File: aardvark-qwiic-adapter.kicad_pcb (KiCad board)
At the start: 2 copper layers, 22.9 x 20.3 mm, 7 parts, among them J1 Conn_02x05_Odd_Even, J2 Conn_01x04, J3 Conn_01x04, J4 Conn_01x02, U1 AP7361C-33E

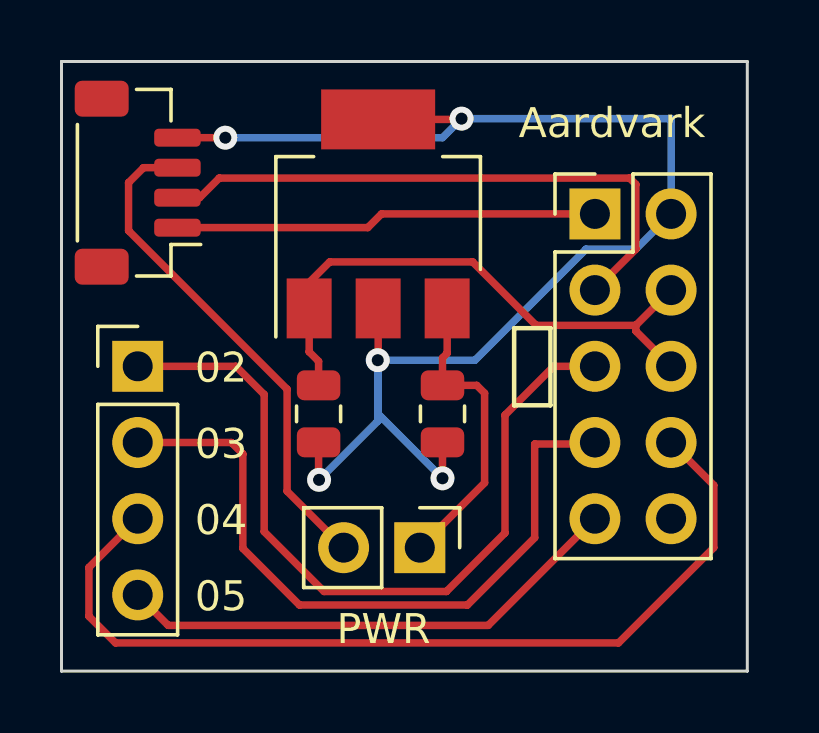
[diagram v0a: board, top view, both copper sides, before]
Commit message: PCB layout tweaks and silkscreen
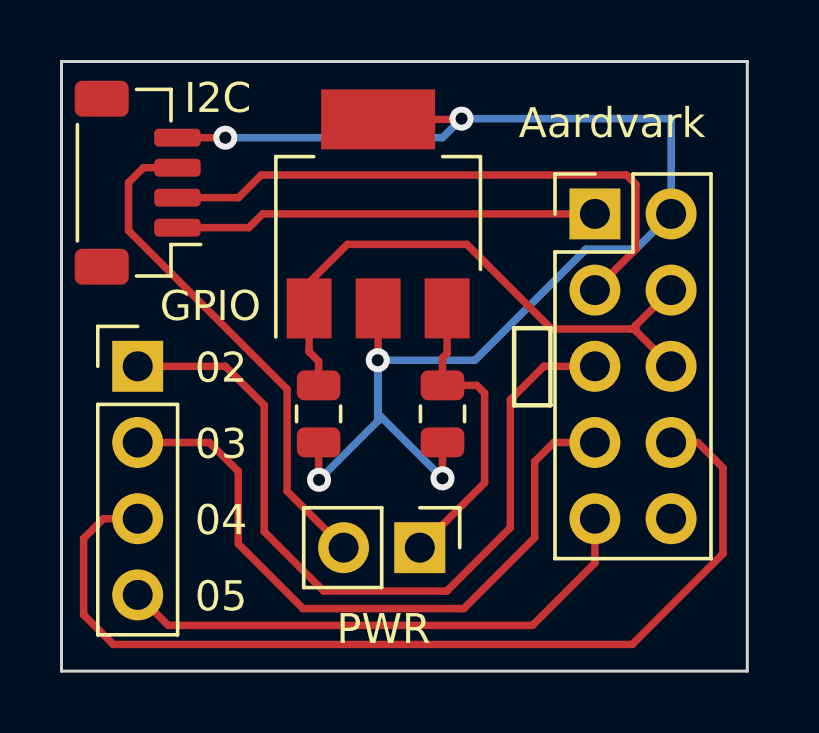
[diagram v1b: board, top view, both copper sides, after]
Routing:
- net /GPIO04: track 30.5 -> 32.5 mm
- net /GPIO05: track 17.1 -> 18.0 mm
- net /GPIO03: track 23.4 -> 22.7 mm
- net +5V: track 19.1 -> 19.7 mm
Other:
- board text added: "GPIO"
- board text added: "I2C"

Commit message: Clean up ground plance
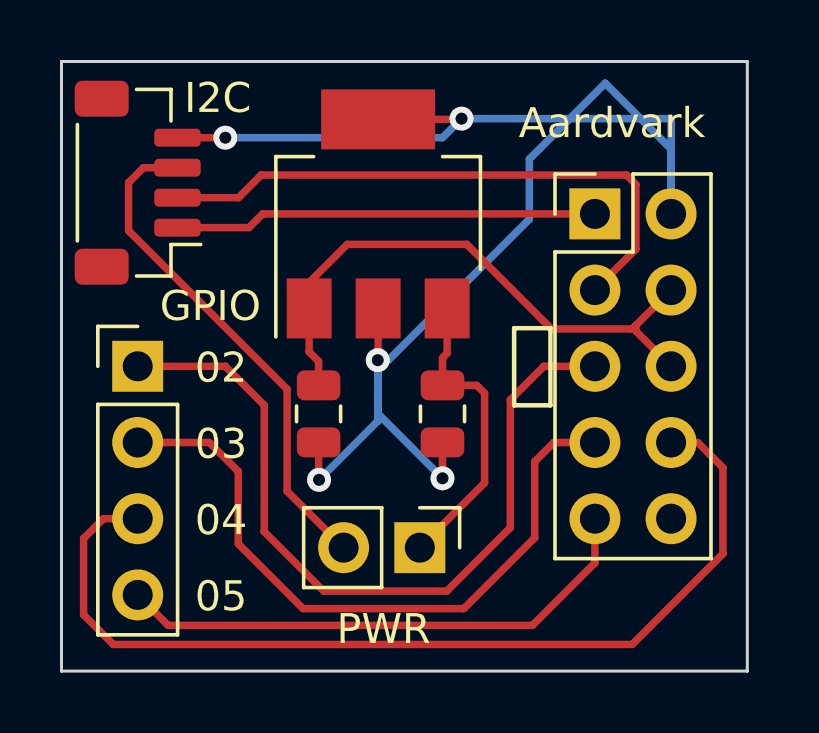
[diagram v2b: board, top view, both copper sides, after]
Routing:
- net GND: track 48.3 -> 54.3 mm
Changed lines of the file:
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@@
   (via (at 119.761 78.74) (size 0.8) (drill 0.4) (layers "F.Cu" "B.Cu") (net 3))
   (via (at 124.841 86.1568) (size 0.8) (drill 0.4) (layers "F.Cu" "B.Cu") (net 3))
+  (segment (start 129.8956 81.4578) (end 129.8956 79.4512) (width 0.25) (layer "B.Cu") (net 3))
   (segment (start 122.8852 90.1446) (end 124.841 88.1888) (width 0.25) (layer "B.Cu") (net 3))
   (segment (start 134.62 78.105) (end 134.62 81.28) (width 0.25) (layer "B.Cu") (net 3))
-  (segment (start 133.445 82.455) (end 134.62 81.28) (width 0.25) (layer "B.Cu") (net 3))
+  (segment (start 129.8956 79.4512) (end 132.4229 76.9239) (width 0.25) (layer "B.Cu") (net 3))
+  (segment (start 134.62 79.121) (end 134.62 81.28) (width 0.25) (layer "B.Cu") (net 3))
   (segment (start 124.841 88.1888) (end 124.841 86.1568) (width 0.25) (layer "B.Cu") (net 3))
+  (segment (start 125.1966 86.1568) (end 129.8956 81.4578) (width 0.25) (layer "B.Cu") (net 3))
+  (segment (start 124.841 86.1568) (end 125.1966 86.1568) (width 0.25) (layer "B.Cu") (net 3))
   (segment (start 127 78.74) (end 127.635 78.105) (width 0.25) (layer "B.Cu") (net 3))
   (segment (start 124.841 87.9348) (end 124.841 86.1568) (width 0.25) (layer "B.Cu") (net 3))
-  (segment (start 124.841 86.1568) (end 128.081499 86.1568) (width 0.25) (layer "B.Cu") (net 3))
   (segment (start 119.761 78.74) (end 127 78.74) (width 0.25) (layer "B.Cu") (net 3))
-  (segment (start 128.081499 86.1568) (end 131.783299 82.455) (width 0.25) (layer "B.Cu") (net 3))
+  (segment (start 132.4229 76.9239) (end 134.62 79.121) (width 0.25) (layer "B.Cu") (net 3))
   (segment (start 127.635 78.105) (end 134.62 78.105) (width 0.25) (layer "B.Cu") (net 3))
   (segment (start 127 90.0938) (end 124.841 87.9348) (width 0.25) (layer "B.Cu") (net 3))
-  (segment (start 131.783299 82.455) (end 133.445 82.455) (width 0.25) (layer "B.Cu") (net 3))
   (segment (start 126.243 92.4052) (end 128.4042 90.244) (width 0.25) (layer "F.Cu") (net 4))
   (segment (start 127.155 85.9256) (end 127.155 84.43) (width 0.25) (layer "F.Cu") (net 4))

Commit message: Tweak layout
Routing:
- net +3.3V: track 10.2 -> 10.9 mm
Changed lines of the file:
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@@
   (segment (start 121.0056 81.28) (end 120.5484 81.7372) (width 0.25) (layer "F.Cu") (net 1))
   (segment (start 120.5484 81.7372) (end 118.1678 81.7372) (width 0.25) (layer "F.Cu") (net 1))
-  (segment (start 132.08 83.82) (end 133.445 82.455) (width 0.25) (layer "F.Cu") (net 2))
+  (segment (start 133.1346 79.9846) (end 120.9548 79.9846) (width 0.25) (layer "F.Cu") (net 2))
+  (segment (start 132.08 83.82) (end 133.35 82.55) (width 0.25) (layer "F.Cu") (net 2))
+  (segment (start 133.35 80.2) (end 133.1346 79.9846) (width 0.25) (layer "F.Cu") (net 2))
+  (segment (start 133.35 82.55) (end 133.35 80.2) (width 0.25) (layer "F.Cu") (net 2))
+  (segment (start 120.9548 79.9846) (end 120.1994 80.74) (width 0.25) (layer "F.Cu") (net 2))
   (segment (start 120.1994 80.74) (end 118.165 80.74) (width 0.25) (layer "F.Cu") (net 2))
-  (segment (start 133.445 82.455) (end 133.445 80.295) (width 0.25) (layer "F.Cu") (net 2))
-  (segment (start 133.1346 79.9846) (end 120.9548 79.9846) (width 0.25) (layer "F.Cu") (net 2))
-  (segment (start 120.9548 79.9846) (end 120.1994 80.74) (width 0.25) (layer "F.Cu") (net 2))
-  (segment (start 133.445 80.295) (end 133.1346 79.9846) (width 0.25) (layer "F.Cu") (net 2))
   (segment (start 118.165 78.74) (end 119.761 78.74) (width 0.25) (layer "F.Cu") (net 3))
   (segment (start 122.87 88.895) (end 122.87 90.1294) (width 0.25) (layer "F.Cu") (net 3))
@@
   (segment (start 127.635 78.105) (end 134.62 78.105) (width 0.25) (layer "B.Cu") (net 3))
   (segment (start 127 90.0938) (end 124.841 87.9348) (width 0.25) (layer "B.Cu") (net 3))
-  (segment (start 126.243 92.4052) (end 128.4042 90.244) (width 0.25) (layer "F.Cu") (net 4))
   (segment (start 127.155 85.9256) (end 127.155 84.43) (width 0.25) (layer "F.Cu") (net 4))
-  (segment (start 128.4042 90.244) (end 128.4042 87.2562) (width 0.25) (layer "F.Cu") (net 4))
-  (segment (start 128.143 86.995) (end 127 86.995) (width 0.25) (layer "F.Cu") (net 4))
+  (segment (start 126.243 92.4052) (end 127.4826 92.4052) (width 0.25) (layer "F.Cu") (net 4))
+  (segment (start 128.4042 91.4836) (end 128.4042 87.2562) (width 0.25) (layer "F.Cu") (net 4))
   (segment (start 127 86.0806) (end 127.155 85.9256) (width 0.25) (layer "F.Cu") (net 4))
   (segment (start 128.4042 87.2562) (end 128.143 86.995) (width 0.25) (layer "F.Cu") (net 4))
+  (segment (start 128.143 86.995) (end 127 86.995) (width 0.25) (layer "F.Cu") (net 4))
+  (segment (start 127.4826 92.4052) (end 128.4042 91.4836) (width 0.25) (layer "F.Cu") (net 4))
   (segment (start 127 86.995) (end 127 86.0806) (width 0.25) (layer "F.Cu") (net 4))
-  (segment (start 121.0564 91.8718) (end 121.0564 87.6554) (width 0.25) (layer "F.Cu") (net 5))
   (segment (start 132.08 86.36) (end 130.3782 86.36) (width 0.25) (layer "F.Cu") (net 5))
+  (segment (start 130.3782 86.36) (end 129.2606 87.4776) (width 0.25) (layer "F.Cu") (net 5))
+  (segment (start 129.2606 87.4776) (end 129.2606 91.7376) (width 0.25) (layer "F.Cu") (net 5))
+  (segment (start 119.761 86.36) (end 116.84 86.36) (width 0.25) (layer "F.Cu") (net 5))
+  (segment (start 123.0376 93.853) (end 120.6246 91.44) (width 0.25) (layer "F.Cu") (net 5))
   (segment (start 129.2606 91.7376) (end 127.1452 93.853) (width 0.25) (layer "F.Cu") (net 5))
-  (segment (start 121.0564 87.6554) (end 119.761 86.36) (width 0.25) (layer "F.Cu") (net 5))
+  (segment (start 120.6246 87.2236) (end 119.761 86.36) (width 0.25) (layer "F.Cu") (net 5))
   (segment (start 127.1452 93.853) (end 123.0376 93.853) (width 0.25) (layer "F.Cu") (net 5))
-  (segment (start 129.2606 87.4776) (end 129.2606 91.7376) (width 0.25) (layer "F.Cu") (net 5))
-  (segment (start 123.0376 93.853) (end 121.0564 91.8718) (width 0.25) (layer "F.Cu") (net 5))
-  (segment (start 130.3782 86.36) (end 129.2606 87.4776) (width 0.25) (layer "F.Cu") (net 5))
-  (segment (start 119.761 86.36) (end 116.84 86.36) (width 0.25) (layer "F.Cu") (net 5))
-  (segment (start 130.0734 89.535) (end 130.0734 92.075) (width 0.25) (layer "F.Cu") (net 6))
-  (segment (start 130.7084 88.9) (end 130.0734 89.535) (width 0.25) (layer "F.Cu") (net 6))
-  (segment (start 120.1928 92.2782) (end 120.1928 89.8652) (width 0.25) (layer "F.Cu") (net 6))
+  (segment (start 120.6246 91.44) (end 120.6246 87.2236) (width 0.25) (layer "F.Cu") (net 5))
+  (segment (start 122.3518 94.4372) (end 119.7864 91.8718) (width 0.25) (layer "F.Cu") (net 6))
+  (segment (start 132.08 88.9) (end 130.7084 88.9) (width 0.25) (layer "F.Cu") (net 6))
   (segment (start 127.7112 94.4372) (end 122.3518 94.4372) (width 0.25) (layer "F.Cu") (net 6))
-  (segment (start 132.08 88.9) (end 130.7084 88.9) (width 0.25) (layer "F.Cu") (net 6))
+  (segment (start 119.7864 91.8718) (end 119.7864 89.4588) (width 0.25) (layer "F.Cu") (net 6))
+  (segment (start 130.048 89.5604) (end 130.048 92.1004) (width 0.25) (layer "F.Cu") (net 6))
   (segment (start 119.2276 88.9) (end 116.84 88.9) (width 0.25) (layer "F.Cu") (net 6))
-  (segment (start 120.1928 89.8652) (end 119.2276 88.9) (width 0.25) (layer "F.Cu") (net 6))
-  (segment (start 130.0734 92.075) (end 127.7112 94.4372) (width 0.25) (layer "F.Cu") (net 6))
-  (segment (start 122.3518 94.4372) (end 120.1928 92.2782) (width 0.25) (layer "F.Cu") (net 6))
+  (segment (start 130.7084 88.9) (end 130.048 89.5604) (width 0.25) (layer "F.Cu") (net 6))
+  (segment (start 130.048 92.1004) (end 127.7112 94.4372) (width 0.25) (layer "F.Cu") (net 6))
+  (segment (start 119.7864 89.4588) (end 119.2276 88.9) (width 0.25) (layer "F.Cu") (net 6))
   (segment (start 134.62 88.9) (end 135.509 88.9) (width 0.25) (layer "F.Cu") (net 7))
   (segment (start 135.509 88.9) (end 136.3472 89.7382) (width 0.25) (layer "F.Cu") (net 7))
@@
   (segment (start 129.9972 94.996) (end 117.856 94.996) (width 0.25) (layer "F.Cu") (net 8))
   (segment (start 132.08 92.9132) (end 129.9972 94.996) (width 0.25) (layer "F.Cu") (net 8))
-  (segment (start 121.82 90.5222) (end 123.703 92.4052) (width 0.25) (layer "F.Cu") (net 9))
-  (segment (start 116.5352 81.8388) (end 121.82 87.1236) (width 0.25) (layer "F.Cu") (net 9))
+  (segment (start 118.165 79.74) (end 117.0338 79.74) (width 0.25) (layer "F.Cu") (net 9))
+  (segment (start 116.5352 81.8388) (end 121.4374 86.741) (width 0.25) (layer "F.Cu") (net 9))
   (segment (start 117.0338 79.74) (end 116.5352 80.2386) (width 0.25) (layer "F.Cu") (net 9))
-  (segment (start 118.165 79.74) (end 117.0338 79.74) (width 0.25) (layer "F.Cu") (net 9))
+  (segment (start 121.4374 86.741) (end 121.4374 90.1396) (width 0.25) (layer "F.Cu") (net 9))
   (segment (start 116.5352 80.2386) (end 116.5352 81.8388) (width 0.25) (layer "F.Cu") (net 9))
-  (segment (start 121.82 87.1236) (end 121.82 90.5222) (width 0.25) (layer "F.Cu") (net 9))
-  (segment (start 123.825 82.296) (end 122.555 83.566) (width 0.25) (layer "F.Cu") (net 10))
+  (segment (start 121.4374 90.1396) (end 123.703 92.4052) (width 0.25) (layer "F.Cu") (net 9))
   (segment (start 134.62 83.82) (end 133.445 84.995) (width 0.25) (layer "F.Cu") (net 10))
+  (segment (start 133.445 84.995) (end 133.3246 85.1154) (width 0.25) (layer "F.Cu") (net 10))
   (segment (start 133.445 85.185) (end 133.445 84.995) (width 0.25) (layer "F.Cu") (net 10))
+  (segment (start 127.8128 82.296) (end 123.2662 82.296) (width 0.25) (layer "F.Cu") (net 10))
   (segment (start 133.3246 85.1154) (end 130.6322 85.1154) (width 0.25) (layer "F.Cu") (net 10))
-  (segment (start 130.6322 85.1154) (end 127.8128 82.296) (width 0.25) (layer "F.Cu") (net 10))
-  (segment (start 127.8128 82.296) (end 123.825 82.296) (width 0.25) (layer "F.Cu") (net 10))
-  (segment (start 133.445 84.995) (end 133.3246 85.1154) (width 0.25) (layer "F.Cu") (net 10))
   (segment (start 134.62 86.36) (end 133.445 85.185) (width 0.25) (layer "F.Cu") (net 10))
   (segment (start 122.555 85.8774) (end 122.555 84.43) (width 0.25) (layer "F.Cu") (net 10))
+  (segment (start 123.2662 82.296) (end 122.555 83.0072) (width 0.25) (layer "F.Cu") (net 10))
   (segment (start 122.87 86.1924) (end 122.555 85.8774) (width 0.25) (layer "F.Cu") (net 10))
-  (segment (start 122.555 83.566) (end 122.555 84.43) (width 0.25) (layer "F.Cu") (net 10))
   (segment (start 122.87 86.995) (end 122.87 86.1924) (width 0.25) (layer "F.Cu") (net 10))
+  (segment (start 122.555 83.0072) (end 122.555 84.43) (width 0.25) (layer "F.Cu") (net 10))
+  (segment (start 130.6322 85.1154) (end 127.8128 82.296) (width 0.25) (layer "F.Cu") (net 10))
   (zone (net 3) (net_name "GND") (layer "B.Cu") (hatch edge 0.5)
     (connect_pads (clearance 0.5))
